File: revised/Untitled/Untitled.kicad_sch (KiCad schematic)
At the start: 42 parts, among them J1 Conn_01x02_Pin, J2 USB_C_Receptacle_USB2.0_16P, J3 ARM Cortex Debug, J4 Conn_Coaxial, J5 Screw_Terminal_01x02, J6 Screw_Terminal_01x02, J7 Screw_Terminal_01x02, Q1 Q_PMOS, Q2 NMOS, Q3 NMOS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

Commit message: signal routing start
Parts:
- added H1, H2, H3, H4: MountingHole_Pad, MountingHole:MountingHole_4.3mm_M4_DIN965_Pad_TopBottom, symbol Mechanical:MountingHole_Pad

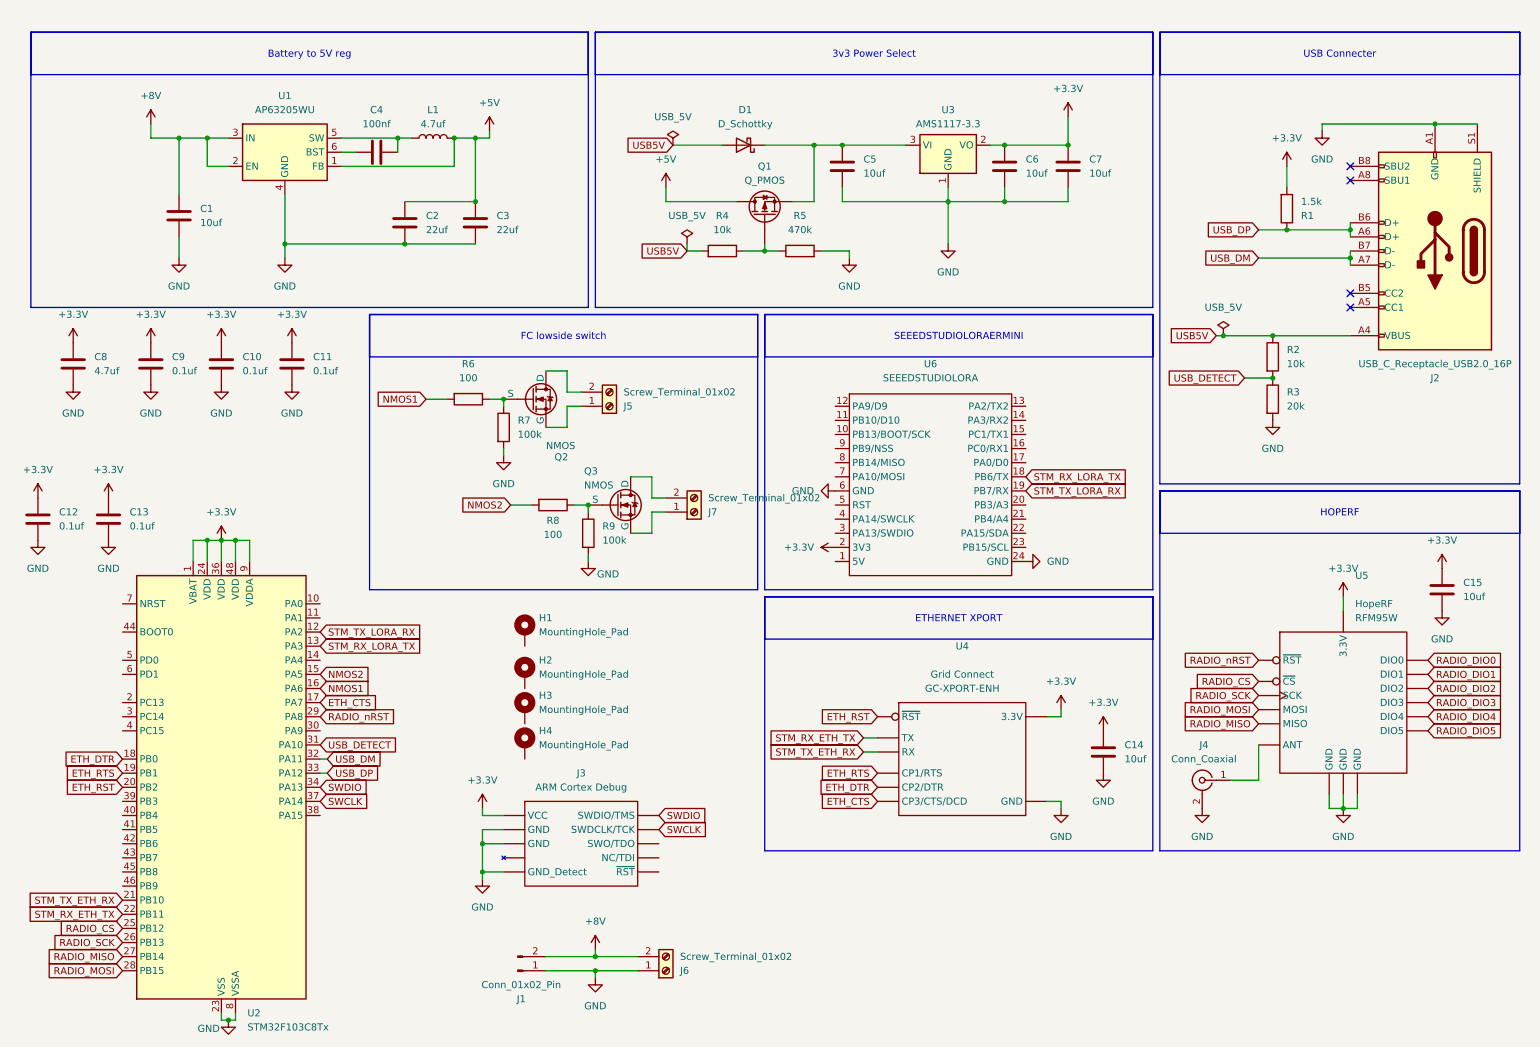
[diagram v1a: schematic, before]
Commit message: optocouplers added
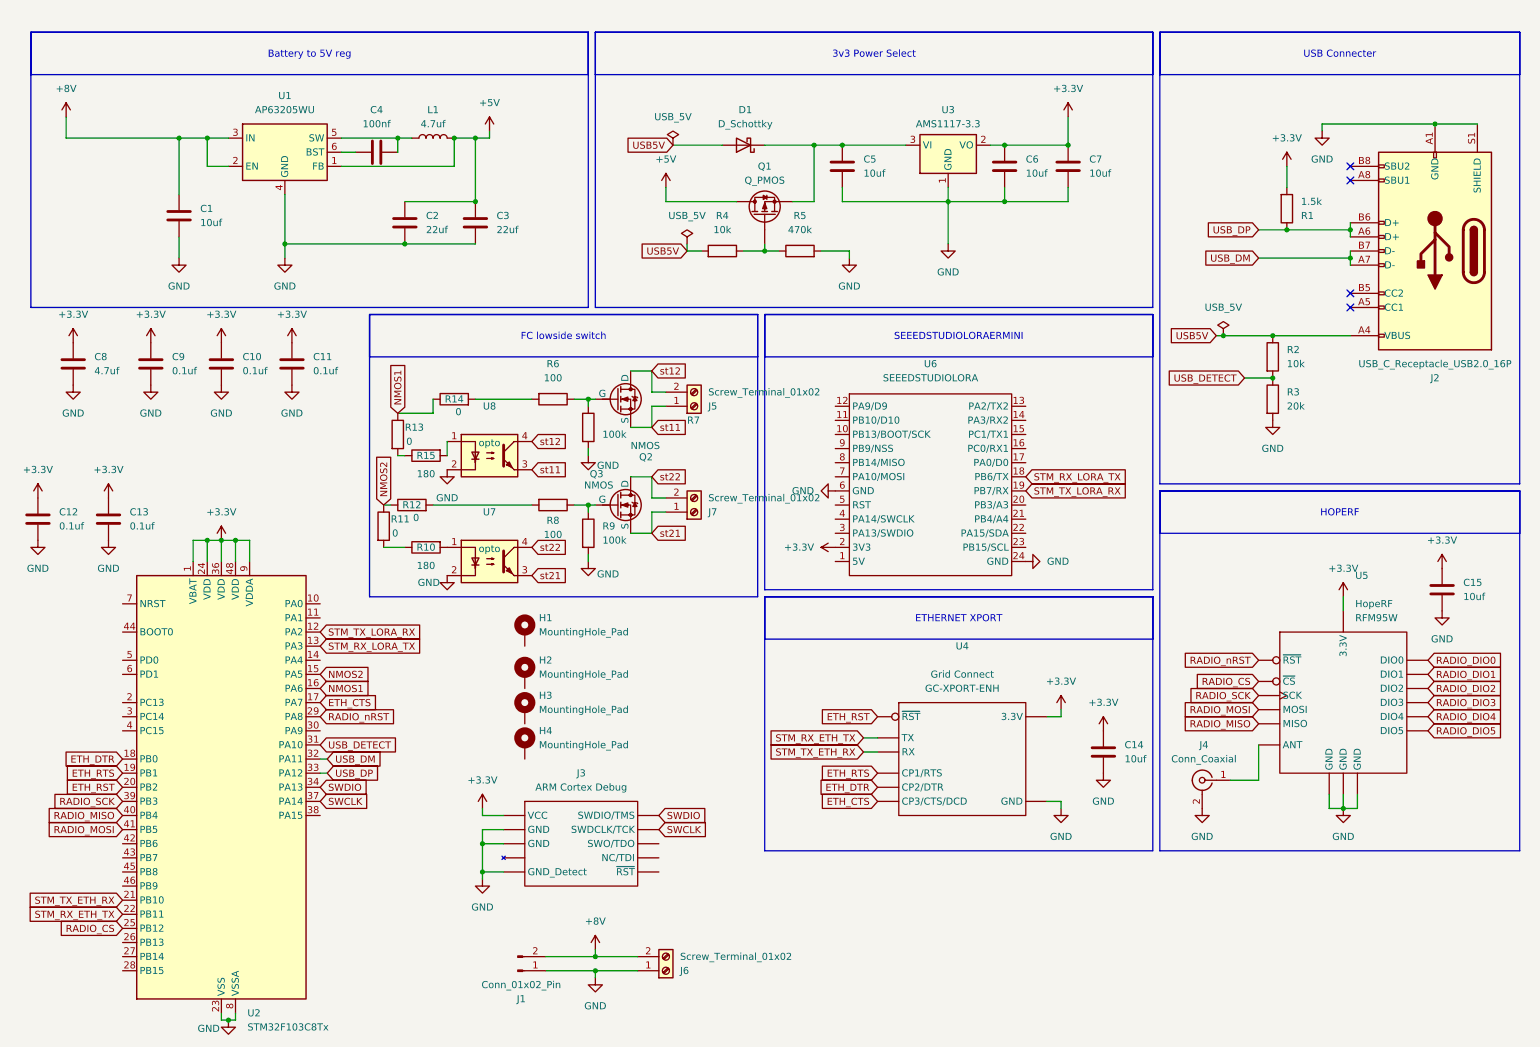
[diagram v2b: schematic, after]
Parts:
- added R10, R15: 180, Resistor_SMD:R_0603_1608Metric_Pad0.98x0.95mm_HandSolder, symbol Device:R
- added R11, R12, R13, R14: 0, Resistor_SMD:R_0603_1608Metric_Pad0.98x0.95mm_HandSolder, symbol Device:R
- added U7, U8: opto, UCIRP-KiCAD-Lib:optocoupler, symbol Isolator:Optocoupler_DC_PhotoNPN_AKEC
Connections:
- net GND: now also U7.2, U8.2
- net NMOS1: now also R13.1, R14.1; no longer R6.2
- net NMOS2: now also R11.1, R12.1; no longer R8.2
- net RADIO_MISO: now also U2.40 (PB4); no longer U2.27 (PB14)
- net RADIO_MOSI: now also U2.41 (PB5); no longer U2.28 (PB15)
- net RADIO_SCK: now also U2.39 (PB3); no longer U2.26 (PB13)
- net at Q3.3 (G): now also R8.1, R9.1; no longer J7.1 (Pin_1)
- net st22: now reaches J7.2 (Pin_2), Q3.1 (D)
- net st22: now also U7.4
- net st12: now reaches J5.2 (Pin_2), Q2.1 (D)
- net st12: now also U8.4
- net at Q2.3 (G): now also R6.1, R7.1; no longer J5.1 (Pin_1)
- new net: R10.1, R11.2
- new net: R10.2, U7.1
- new net: R13.2, R15.1
- new net: R12.2, R8.2
- new net: R14.2, R6.2
- new net: R15.2, U8.1
- new net st11: J5.1 (Pin_1), Q2.4 (S), U8.3
- new net st21: J7.1 (Pin_1), Q3.4 (S), U7.3
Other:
- moved on the sheet: J5, Q2, Q3, R6, R7

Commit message: cleaned up layout and board shape finalized
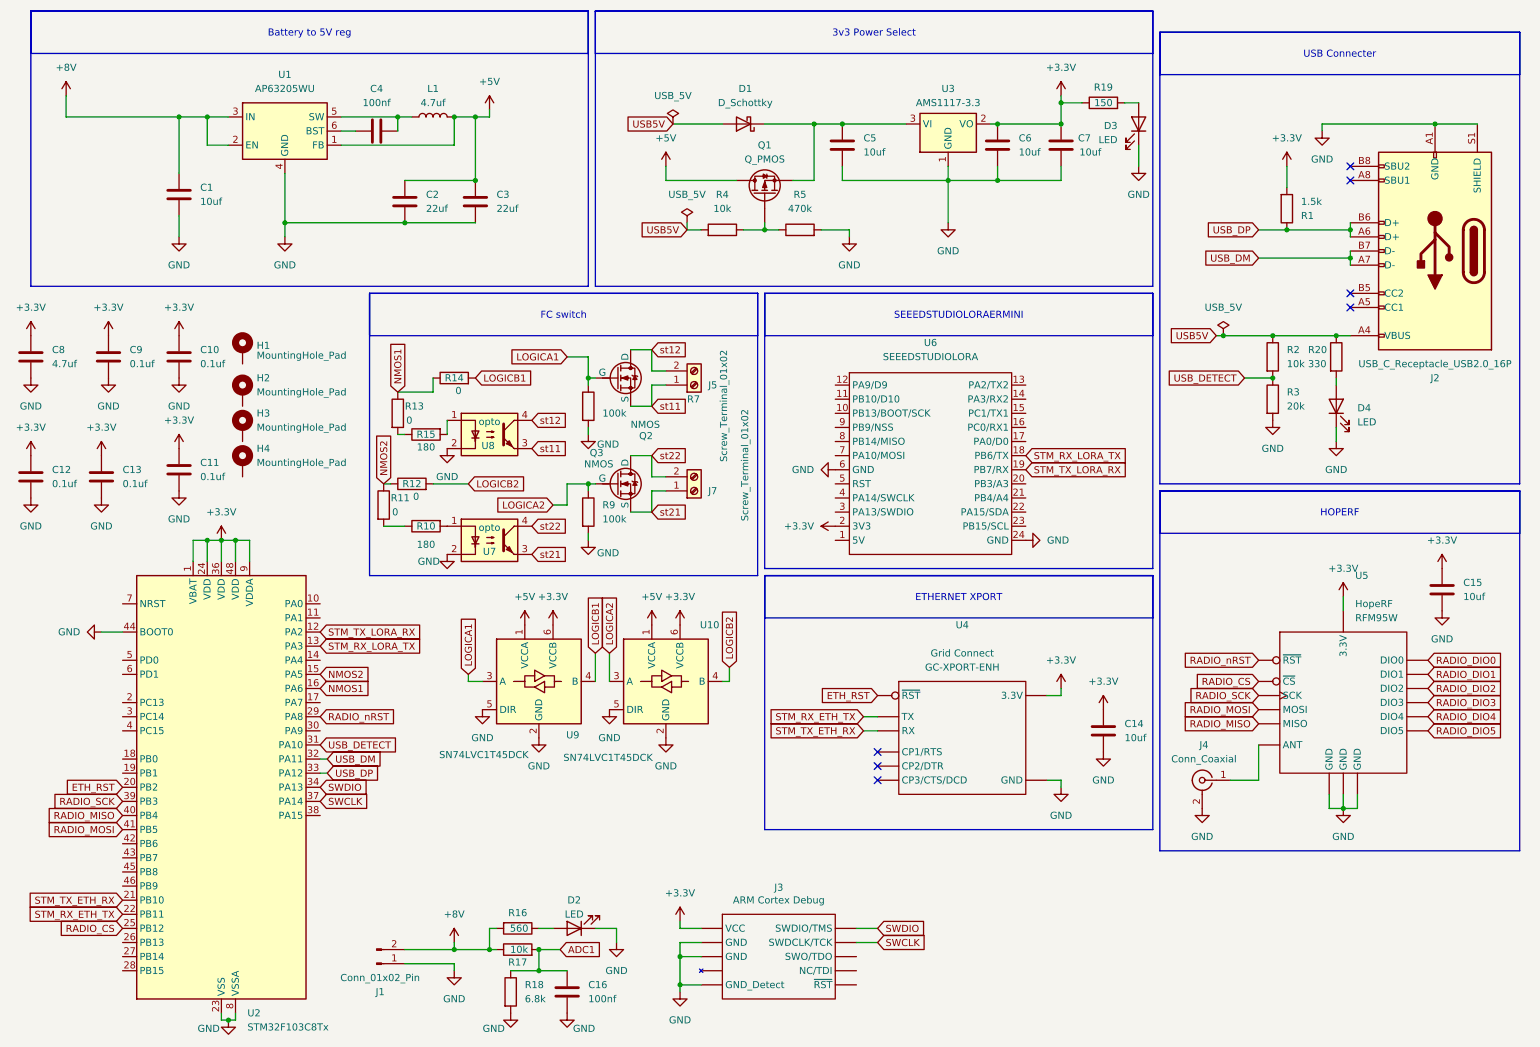
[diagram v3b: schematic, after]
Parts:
- removed J6: Screw_Terminal_01x02, TerminalBlock_Phoenix:TerminalBlock_Phoenix_MKDS-1,5-2-5.08_1x02_P5.08mm_Horizontal, symbol Connector:Screw_Terminal_01x02
- removed R6, R8: 100, Resistor_SMD:R_0603_1608Metric_Pad0.98x0.95mm_HandSolder, symbol Device:R
- added C16: 100nf, Capacitor_SMD:C_0603_1608Metric_Pad1.08x0.95mm_HandSolder, symbol Device:C
- added D2, D3, D4: LED, Resistor_SMD:R_0603_1608Metric_Pad0.98x0.95mm_HandSolder, symbol Device:LED
- added R16: 560, Resistor_SMD:R_0603_1608Metric_Pad0.98x0.95mm_HandSolder, symbol Device:R
- added R17: 10k, Resistor_SMD:R_0603_1608Metric_Pad0.98x0.95mm_HandSolder, symbol Device:R
- added R18: 6.8k, Resistor_SMD:R_0603_1608Metric_Pad0.98x0.95mm_HandSolder, symbol Device:R
- added R19: 150, Resistor_SMD:R_0603_1608Metric_Pad0.98x0.95mm_HandSolder, symbol Device:R
- added R20: 330, Resistor_SMD:R_0603_1608Metric_Pad0.98x0.95mm_HandSolder, symbol Device:R
- added U10, U9: SN74LVC1T45DCK, Package_TO_SOT_SMD:SOT-363_SC-70-6, symbol Logic_LevelTranslator:SN74LVC1T45DCK
- J4: footprint Connector_Coaxial:SMA_Molex_73251-2120_EdgeMount_Horizontal -> UCIRP-KiCAD-Lib:CONN_73391-0070_MOL
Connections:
- net +3.3V: now also R19.1, U10.6 (VCCB), U9.6 (VCCB)
- net +5V: now also U10.1 (VCCA), U9.1 (VCCA)
- net +8V: now also R16.2, R17.1
- net GND: now also U2.44 (BOOT0), C16.2, D2.1 (K), D3.1 (K), D4.1 (K), R18.2, U10.2 (GND), U10.5 (DIR), U9.2 (GND), U9.5 (DIR)
- net USB5V: now also R20.1
- net LOGICB2: now reaches R12.2
- net LOGICB2: now also U10.4 (B)
- net LOGICA2: now reaches Q3.3 (G), R9.1
- net LOGICA2: now also U10.3 (A)
- net LOGICB1: now reaches R14.2
- net LOGICB1: now also U9.4 (B)
- net LOGICA1: now reaches Q2.3 (G), R7.1
- net LOGICA1: now also U9.3 (A)
- net ETH_CTS: no longer names the net of U2.17 (PA7)
- net ETH_CTS: no longer U4.8 (CP3/CTS/DCD)
- net ETH_DTR: no longer names the net of U2.18 (PB0)
- net ETH_DTR: no longer U4.7 (CP2/DTR)
- net ETH_RTS: no longer names the net of U2.19 (PB1)
- net ETH_RTS: no longer U4.6 (CP1/RTS)
- new net: D2.2 (A), R16.1
- new net: D3.2 (A), R19.2
- new net: D4.2 (A), R20.2
- new net ADC1: C16.1, R17.2, R18.1
- no-connect marks 4 -> 7
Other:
- moved on the sheet: C1, C10, C11, C12, C13, C14, C2, C3, C4, C5, C6, C7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

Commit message: prereview board
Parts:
- added Y1: 16MHz, Crystal:Crystal_SMD_2016-4Pin_2.0x1.6mm, symbol UCIRP-KiCAD-Lib:Crystal_GND24_Small
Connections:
- net +3.3V: now also Y1.4
- net GND: now also Y1.2
- net at U2.5 (PD0): now also Y1.3
- no-connect marks 7 -> 8
